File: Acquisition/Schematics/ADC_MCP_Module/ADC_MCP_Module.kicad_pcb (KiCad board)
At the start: 2 copper layers, 20 x 26.8 mm, 39 parts, among them J1 Can, J2 AudioJack4_SwitchTR1, J3 Conn_02x06_Counter_Clockwise, Q1 IRLML9301, SW1 SW_DIP_x01

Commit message: Added first version of main board
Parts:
- removed R17: 470R, Resistor_SMD:R_0603_1608Metric
- removed R18, R19: 0, Resistor_SMD:R_0603_1608Metric
- removed R6: 10k, Resistor_SMD:R_0603_1608Metric
- moved R1 1.59 mm to (94.9, 84.3)
- moved C11 1.57 mm to (93.5, 81.3), turned to 0 degrees
- moved J2 0.82 mm to (102.9, 74.2)
- moved R10 0.51 mm to (108.0, 87.4)
- moved R11 0.51 mm to (108.0, 84.3)
- moved C2 0.38 mm to (97.6, 94.7)
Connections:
- J3 pad 11: /IRQ_Sel -> /nIRQ
- J3 pad 5: /Out -> /SDI
- J3 pad 8: /SDI -> /Out
- R13 pad 1: /SDO -> /Out
- U1 pad 10: Net-(U1-Ctrl34) -> unconnected-(U1-Ctrl34-Pad10)
- U1 pad 7: /nIRQ -> unconnected-(U1-In3_1-Pad7)
- U1 pad 8: Net-(U1-Out3) -> unconnected-(U1-Out3-Pad8)
- U1 pad 9: /SDO -> unconnected-(U1-In3_0-Pad9)
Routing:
- net GND: track 80.5 -> 131.9 mm, vias 8 -> 14
- net /nIRQ: track 29.8 -> 55.9 mm, vias 2 -> 4
- net +3.3V: track 70.7 -> 75.8 mm
- net /IN_Ctrl: track 11.8 -> 14.7 mm
- net /DIV1: track 13.5 -> 10.9 mm
- net /DIV2: track 4.63 -> 3.64 mm
- net /REFIN-: track 17.1 -> 17.8 mm
- net /Out: track 4.37 -> 4.96 mm
- net /SDI: track 5.04 -> 4.62 mm, vias 0 -> 1
- net /SDO: track 0.13 -> 0.00 mm, vias 1 -> 0
- added copper zone on B.Cu, net GND
- added copper zone on F.Cu, net GND
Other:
- board size 20 x 26.8 mm -> 18 x 26.8 mm

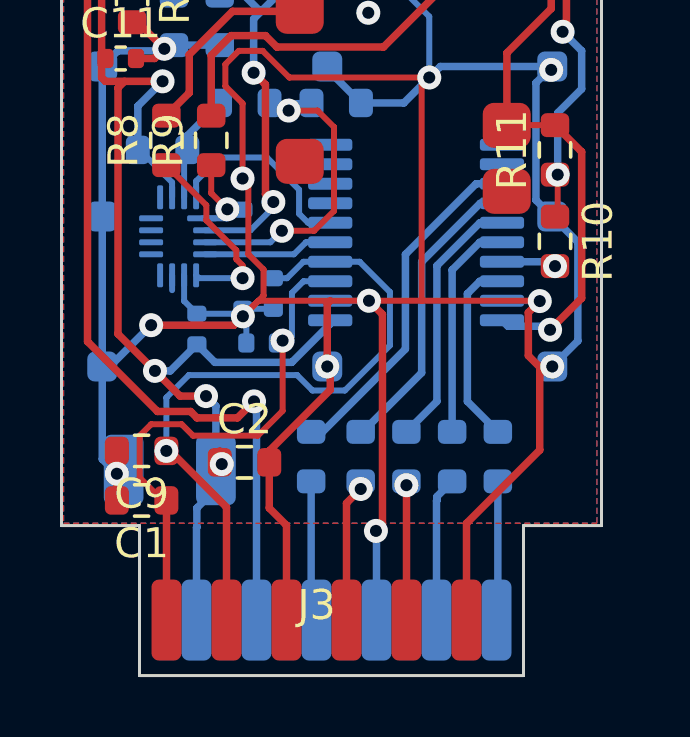
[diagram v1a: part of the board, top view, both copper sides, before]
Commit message: ADC board prototype - ORDER
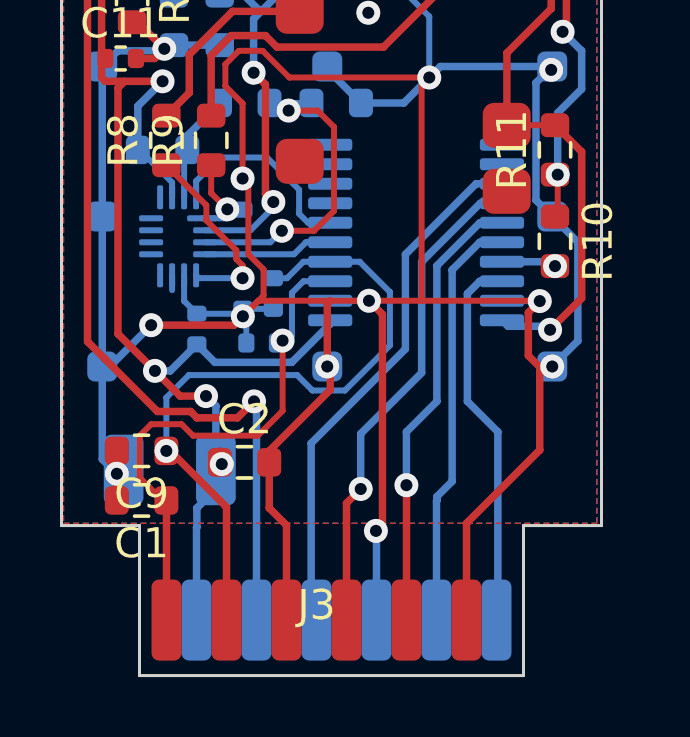
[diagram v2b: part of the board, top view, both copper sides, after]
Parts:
- removed R12, R13, R14, R15, R16: 10, Resistor_SMD:R_0603_1608Metric
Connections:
- U2 pad 13: Net-(U2-nCS) -> /nCS
- U2 pad 14: Net-(U2-SCK) -> /SCK
- U2 pad 15: Net-(U2-SDI) -> /SDI
- U2 pad 16: Net-(U2-SDO) -> /Out
- U2 pad 18: Net-(U2-MCLK) -> /MCLK
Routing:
- net /nCS: track 4.70 -> 17.8 mm
- net /SCK: track 4.82 -> 16.5 mm
- net Net-(U2-nCS): track 11.6 -> 0.00 mm
- net /SDI: track 4.62 -> 15.0 mm
- net Net-(U2-SCK): track 10.1 -> 0.00 mm
- net /Out: track 4.96 -> 13.9 mm
- net Net-(U2-SDI): track 8.72 -> 0.00 mm
- net /MCLK: track 4.64 -> 12.6 mm
- net Net-(U2-SDO): track 7.44 -> 0.00 mm
- net Net-(U2-MCLK): track 6.35 -> 0.00 mm
